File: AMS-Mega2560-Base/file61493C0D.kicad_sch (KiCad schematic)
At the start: 50 parts, among them IC10 LM2597MX-ADJ_NOPB, IC11 LM2597M-3.3_NOPB, IC12 OPA2340PA, IC9 LM2670SX-5.0_NOPB, J21 Screw_Terminal_01x03, J22 Conn_01x07, Q21 IRF9Z34NPBF, Q22 BD140, Q23 2N7000, Q5 2N7000, Q6 IRF9Z34NPBF, U1 BK_HTC-15M, U2 TL431LP

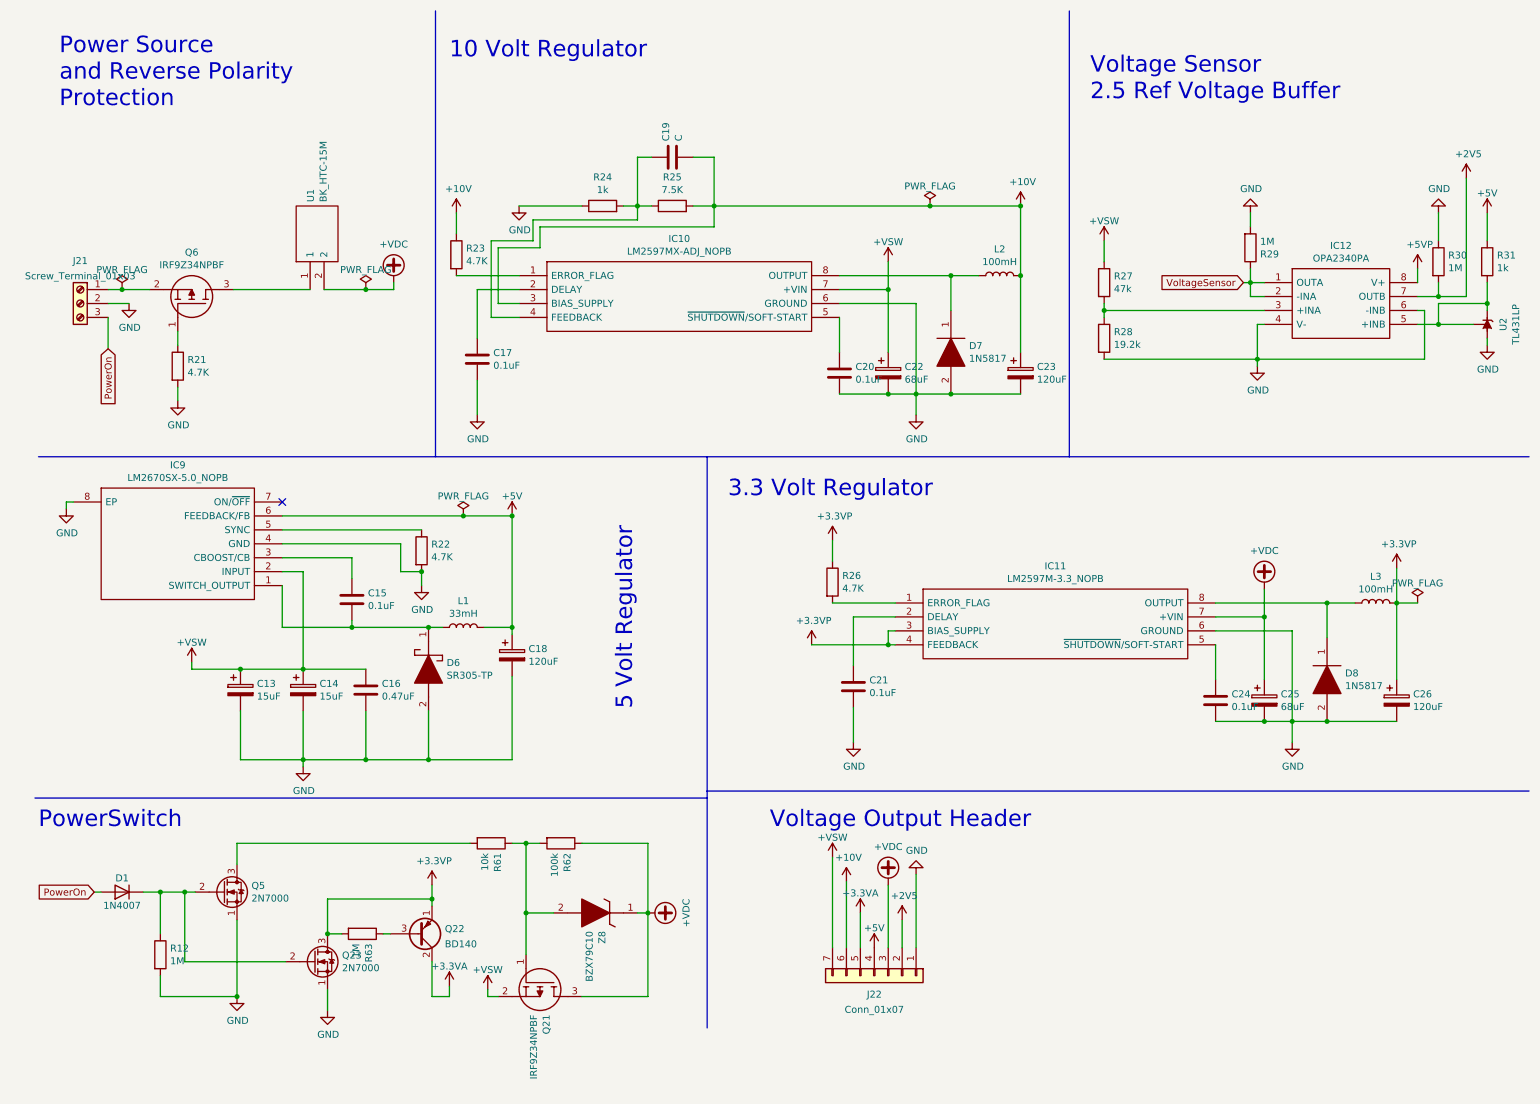
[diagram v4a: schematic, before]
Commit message: cleared all of the ERC stuff need to go over some of the power stuff for this before finishing routing.
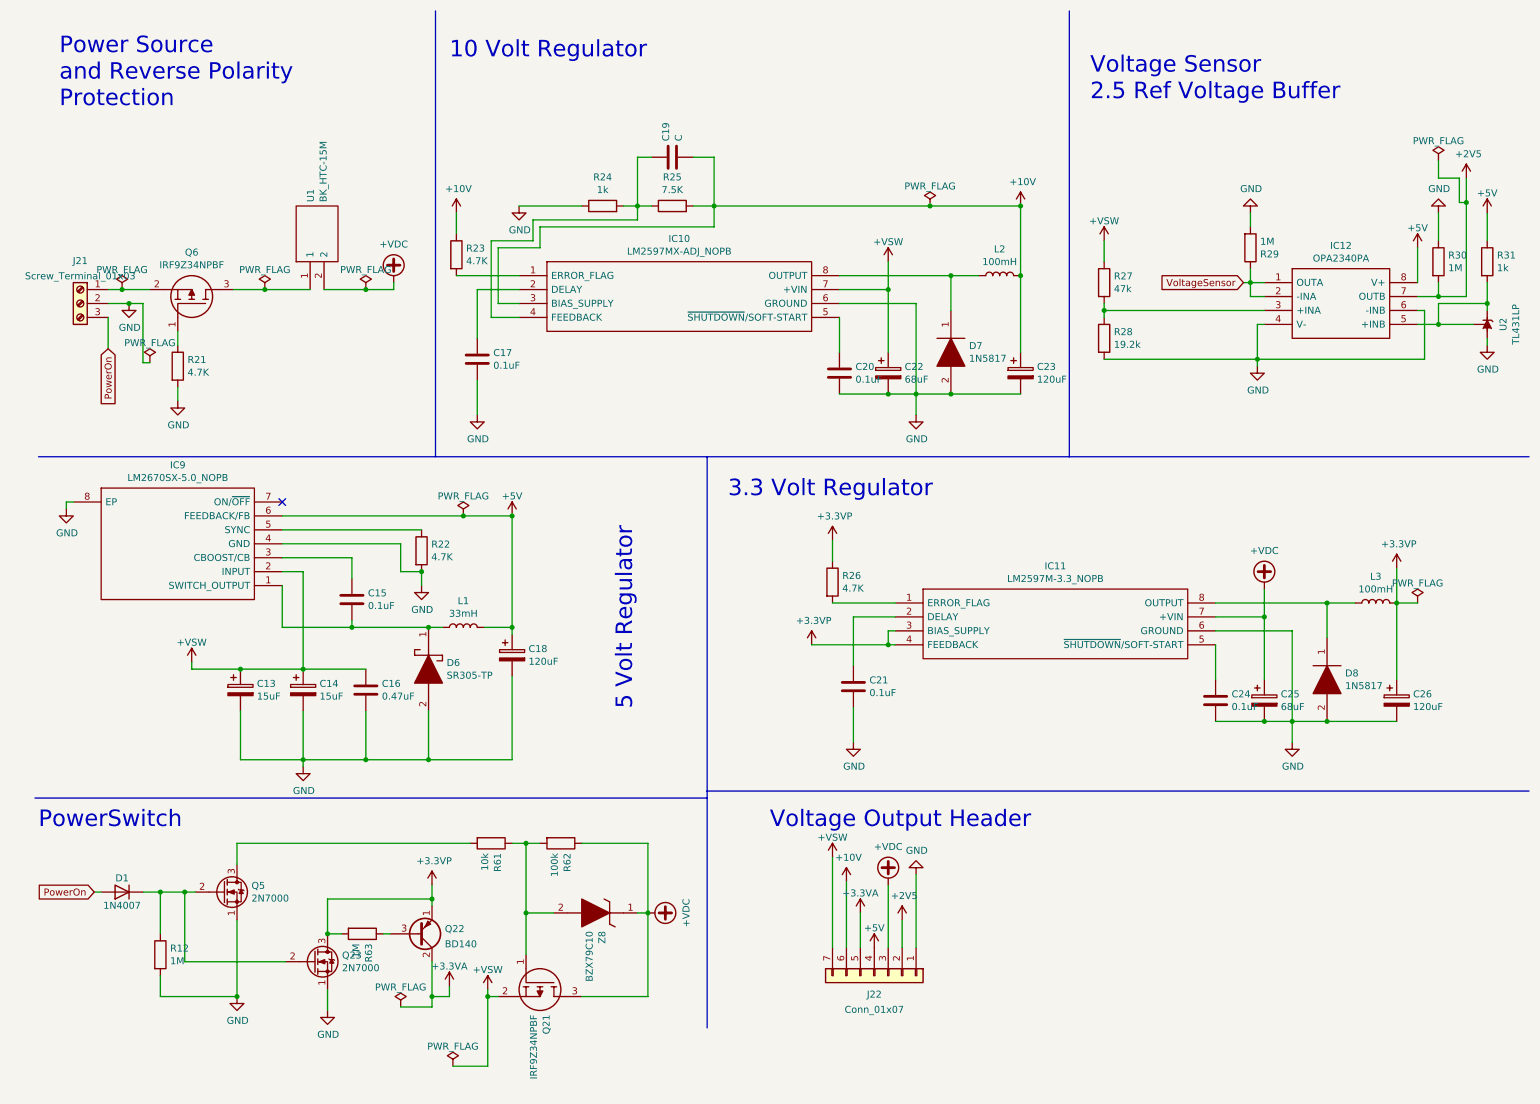
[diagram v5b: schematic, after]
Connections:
- net +5VP is gone; now on net +5V: IC12.8 (V+)
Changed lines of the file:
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@@
   (junction (at 234.95 76.2) (diameter 0) (color 0 0 0 0)
   )
+  (junction (at 53.975 63.5) (diameter 0) (color 0 0 0 0)
+  )
   (junction (at 34.925 173.355) (diameter 0) (color 0 0 0 0)
   )
+  (junction (at 273.05 47.625) (diameter 0) (color 0 0 0 0)
+  )
   (junction (at 83.82 149.225) (diameter 0) (color 0 0 0 0)
   )
@@
   (junction (at 236.22 123.19) (diameter 0) (color 0 0 0 0)
   )
+  (junction (at 84.455 192.405) (diameter 0) (color 0 0 0 0)
+  )
   (junction (at 90.17 104.775) (diameter 0) (color 0 0 0 0)
   )
@@
   (junction (at 121.92 48.26) (diameter 0) (color 0 0 0 0)
   )
+  (junction (at 29.21 66.04) (diameter 0) (color 0 0 0 0)
+  )
   (junction (at 60.96 132.715) (diameter 0) (color 0 0 0 0)
   )
@@
   )
   (junction (at 179.07 82.55) (diameter 0) (color 0 0 0 0)
+  )
+  (junction (at 94.615 192.405) (diameter 0) (color 0 0 0 0)
   )
   (junction (at 172.72 82.55) (diameter 0) (color 0 0 0 0)
@@
     (stroke (width 0) (type default) (color 0 0 0 0))
   )
+  (wire (pts (xy 31.75 76.835) (xy 31.75 66.04))
+    (stroke (width 0) (type default) (color 0 0 0 0))
+  )
   (wire (pts (xy 121.92 48.26) (xy 119.38 48.26))
     (stroke (width 0) (type default) (color 0 0 0 0))
@@
     (stroke (width 0) (type default) (color 0 0 0 0))
   )
-  (wire (pts (xy 48.26 63.5) (xy 62.23 63.5))
+  (wire (pts (xy 48.26 63.5) (xy 53.975 63.5))
+    (stroke (width 0) (type default) (color 0 0 0 0))
+  )
+  (wire (pts (xy 53.975 63.5) (xy 62.23 63.5))
     (stroke (width 0) (type default) (color 0 0 0 0))
   )
@@
     (stroke (width 0) (type default) (color 0 0 0 0))
   )
+  (wire (pts (xy 31.75 66.04) (xy 29.21 66.04))
+    (stroke (width 0) (type default) (color 0 0 0 0))
+  )
   (wire (pts (xy 121.92 48.26) (xy 121.92 50.8))
     (stroke (width 0) (type default) (color 0 0 0 0))
@@
     (stroke (width 0) (type default) (color 0 0 0 0))
   )
+  (wire (pts (xy 78.74 194.31) (xy 84.455 194.31))
+    (stroke (width 0) (type default) (color 0 0 0 0))
+  )
   (polyline (pts (xy 134.62 154.94) (xy 284.48 154.94))
     (stroke (width 0) (type default) (color 0 0 0 0))
@@
     (stroke (width 0) (type default) (color 0 0 0 0))
   )
-  (wire (pts (xy 264.16 62.23) (xy 264.16 59.69))
+  (wire (pts (xy 264.16 55.88) (xy 264.16 62.23))
     (stroke (width 0) (type default) (color 0 0 0 0))
   )
@@
     (stroke (width 0) (type default) (color 0 0 0 0))
   )
-  (wire (pts (xy 273.05 64.77) (xy 273.05 43.18))
+  (wire (pts (xy 273.05 64.77) (xy 273.05 47.625))
     (stroke (width 0) (type default) (color 0 0 0 0))
   )
@@
     (stroke (width 0) (type default) (color 0 0 0 0))
   )
+  (wire (pts (xy 271.78 47.625) (xy 273.05 47.625))
+    (stroke (width 0) (type default) (color 0 0 0 0))
+  )
   (wire (pts (xy 101.6 184.785) (xy 101.6 177.165))
     (stroke (width 0) (type default) (color 0 0 0 0))
@@
     (stroke (width 0) (type default) (color 0 0 0 0))
   )
+  (wire (pts (xy 84.455 194.31) (xy 84.455 192.405))
+    (stroke (width 0) (type default) (color 0 0 0 0))
+  )
   (wire (pts (xy 274.32 69.85) (xy 267.97 69.85))
     (stroke (width 0) (type default) (color 0 0 0 0))
@@
     (stroke (width 0) (type default) (color 0 0 0 0))
   )
+  (wire (pts (xy 273.05 47.625) (xy 273.05 43.18))
+    (stroke (width 0) (type default) (color 0 0 0 0))
+  )
   (wire (pts (xy 234.95 76.2) (xy 265.43 76.2))
     (stroke (width 0) (type default) (color 0 0 0 0))
@@
     (stroke (width 0) (type default) (color 0 0 0 0))
   )
+  (wire (pts (xy 267.97 40.005) (xy 267.97 43.18))
+    (stroke (width 0) (type default) (color 0 0 0 0))
+  )
   (wire (pts (xy 162.56 177.165) (xy 162.56 183.515))
     (stroke (width 0) (type default) (color 0 0 0 0))
@@
     (stroke (width 0) (type default) (color 0 0 0 0))
   )
+  (wire (pts (xy 267.97 43.18) (xy 271.78 43.18))
+    (stroke (width 0) (type default) (color 0 0 0 0))
+  )
   (wire (pts (xy 48.895 164.465) (xy 91.44 164.465))
     (stroke (width 0) (type default) (color 0 0 0 0))
@@
     (stroke (width 0) (type default) (color 0 0 0 0))
   )
+  (wire (pts (xy 88.265 205.105) (xy 94.615 205.105))
+    (stroke (width 0) (type default) (color 0 0 0 0))
+  )
   (wire (pts (xy 48.895 164.465) (xy 48.895 168.275))
     (stroke (width 0) (type default) (color 0 0 0 0))
@@
     (stroke (width 0) (type default) (color 0 0 0 0))
   )
+  (wire (pts (xy 271.78 43.18) (xy 271.78 47.625))
+    (stroke (width 0) (type default) (color 0 0 0 0))
+  )
   (wire (pts (xy 260.35 134.62) (xy 260.35 120.65))
     (stroke (width 0) (type default) (color 0 0 0 0))
@@
     (stroke (width 0) (type default) (color 0 0 0 0))
   )
+  (wire (pts (xy 94.615 205.105) (xy 94.615 192.405))
+    (stroke (width 0) (type default) (color 0 0 0 0))
+  )
   (wire (pts (xy 207.01 67.31) (xy 236.22 67.31))
     (stroke (width 0) (type default) (color 0 0 0 0))
@@
   )
   (wire (pts (xy 99.06 149.225) (xy 99.06 133.985))
+    (stroke (width 0) (type default) (color 0 0 0 0))
+  )
+  (wire (pts (xy 33.02 76.835) (xy 31.75 76.835))
     (stroke (width 0) (type default) (color 0 0 0 0))
   )
@@
     (pin "1")
   )
-  (symbol (lib_id "power:+5VP") (at 264.16 59.69 0) (unit 1)
-    (in_bom yes) (on_board yes)
-    (property "Reference" "#PWR082" (id 0) (at 264.16 63.5 0)
-      (effects (font (size 1.27 1.27)) hide)
-    )
-    (property "Value" "+5VP" (id 1) (at 264.541 55.2958 0))
-    (property "Footprint" "" (id 2) (at 264.16 59.69 0)
-      (effects (font (size 1.27 1.27)) hide)
-    )
-    (property "Datasheet" "" (id 3) (at 264.16 59.69 0)
-      (effects (font (size 1.27 1.27)) hide)
-    )
-    (pin "1")
-  )
   (symbol (lib_id "power:GND") (at 234.95 77.47 0) (unit 1)
     (in_bom yes) (on_board yes)
@@
     (pin "8")
   )
+  (symbol (lib_id "power:PWR_FLAG") (at 88.265 205.105 0) (unit 1)
+    (in_bom yes) (on_board yes) (fields_autoplaced)
+    (property "Reference" "#FLG0102" (id 0) (at 88.265 203.2 0)
+      (effects (font (size 1.27 1.27)) hide)
+    )
+    (property "Value" "PWR_FLAG" (id 1) (at 88.265 201.5005 0))
+    (property "Footprint" "" (id 2) (at 88.265 205.105 0)
+      (effects (font (size 1.27 1.27)) hide)
+    )
+    (property "Datasheet" "~" (id 3) (at 88.265 205.105 0)
+      (effects (font (size 1.27 1.27)) hide)
+    )
+    (pin "1")
+  )
   (symbol (lib_id "Transistor_FET:2N7000") (at 46.355 173.355 0) (unit 1)
     (in_bom yes) (on_board yes)
@@
     (pin "3")
   )
+  (symbol (lib_id "power:PWR_FLAG") (at 267.97 40.005 0) (unit 1)
+    (in_bom yes) (on_board yes) (fields_autoplaced)
+    (property "Reference" "#FLG0101" (id 0) (at 267.97 38.1 0)
+      (effects (font (size 1.27 1.27)) hide)
+    )
+    (property "Value" "PWR_FLAG" (id 1) (at 267.97 36.4005 0))
+    (property "Footprint" "" (id 2) (at 267.97 40.005 0)
+      (effects (font (size 1.27 1.27)) hide)
+    )
+    (property "Datasheet" "~" (id 3) (at 267.97 40.005 0)
+      (effects (font (size 1.27 1.27)) hide)
+    )
+    (pin "1")
+  )
   (symbol (lib_id "Transistor_FET:2N7000") (at 62.865 186.055 0) (unit 1)
     (in_bom yes) (on_board yes)
@@
     (pin "1")
     (pin "2")
+  )
+  (symbol (lib_id "power:PWR_FLAG") (at 78.74 194.31 0) (unit 1)
+    (in_bom yes) (on_board yes) (fields_autoplaced)
+    (property "Reference" "#FLG01" (id 0) (at 78.74 192.405 0)
+      (effects (font (size 1.27 1.27)) hide)
+    )
+    (property "Value" "PWR_FLAG" (id 1) (at 78.74 190.7055 0))
+    (property "Footprint" "" (id 2) (at 78.74 194.31 0)
+      (effects (font (size 1.27 1.27)) hide)
+    )
+    (property "Datasheet" "~" (id 3) (at 78.74 194.31 0)
+      (effects (font (size 1.27 1.27)) hide)
+    )
+    (pin "1")
   )
   (symbol (lib_id "power:GND") (at 48.895 192.405 0) (unit 1)
@@
     (pin "1")
   )
+  (symbol (lib_id "power:PWR_FLAG") (at 33.02 76.835 0) (unit 1)
+    (in_bom yes) (on_board yes) (fields_autoplaced)
+    (property "Reference" "#FLG0104" (id 0) (at 33.02 74.93 0)
+      (effects (font (size 1.27 1.27)) hide)
+    )
+    (property "Value" "PWR_FLAG" (id 1) (at 33.02 73.2305 0))
+    (property "Footprint" "" (id 2) (at 33.02 76.835 0)
+      (effects (font (size 1.27 1.27)) hide)
+    )
+    (property "Datasheet" "~" (id 3) (at 33.02 76.835 0)
+      (effects (font (size 1.27 1.27)) hide)
+    )
+    (pin "1")
+  )
   (symbol (lib_id "Device:R") (at 34.925 184.785 0) (unit 1)
     (in_bom yes) (on_board yes)
@@
     (pin "1")
   )
+  (symbol (lib_id "power:PWR_FLAG") (at 53.975 63.5 0) (unit 1)
+    (in_bom yes) (on_board yes) (fields_autoplaced)
+    (property "Reference" "#FLG0103" (id 0) (at 53.975 61.595 0)
+      (effects (font (size 1.27 1.27)) hide)
+    )
+    (property "Value" "PWR_FLAG" (id 1) (at 53.975 59.8955 0))
+    (property "Footprint" "" (id 2) (at 53.975 63.5 0)
+      (effects (font (size 1.27 1.27)) hide)
+    )
+    (property "Datasheet" "~" (id 3) (at 53.975 63.5 0)
+      (effects (font (size 1.27 1.27)) hide)
+    )
+    (pin "1")
+  )
   (symbol (lib_id "Device:R") (at 95.25 164.465 270) (unit 1)
     (in_bom yes) (on_board yes)
@@
       (effects (font (size 1.27 1.27)) hide)
     )
+    (pin "1")
+  )
+  (symbol (lib_id "power:+5V") (at 264.16 55.88 0) (unit 1)
+    (in_bom yes) (on_board yes) (fields_autoplaced)
+    (property "Reference" "#PWR0102" (id 0) (at 264.16 59.69 0)
+      (effects (font (size 1.27 1.27)) hide)
+    )
+    (property "Value" "+5V" (id 1) (at 264.16 52.2755 0))
+    (property "Footprint" "" (id 2) (at 264.16 55.88 0)
+      (effects (font (size 1.27 1.27)) hide)
+    )
+    (property "Datasheet" "" (id 3) (at 264.16 55.88 0)
+      (effects (font (size 1.27 1.27)) hide)
+    )
